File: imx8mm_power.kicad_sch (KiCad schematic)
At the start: 4 parts, among them U3 MT40A1G16KD-062E

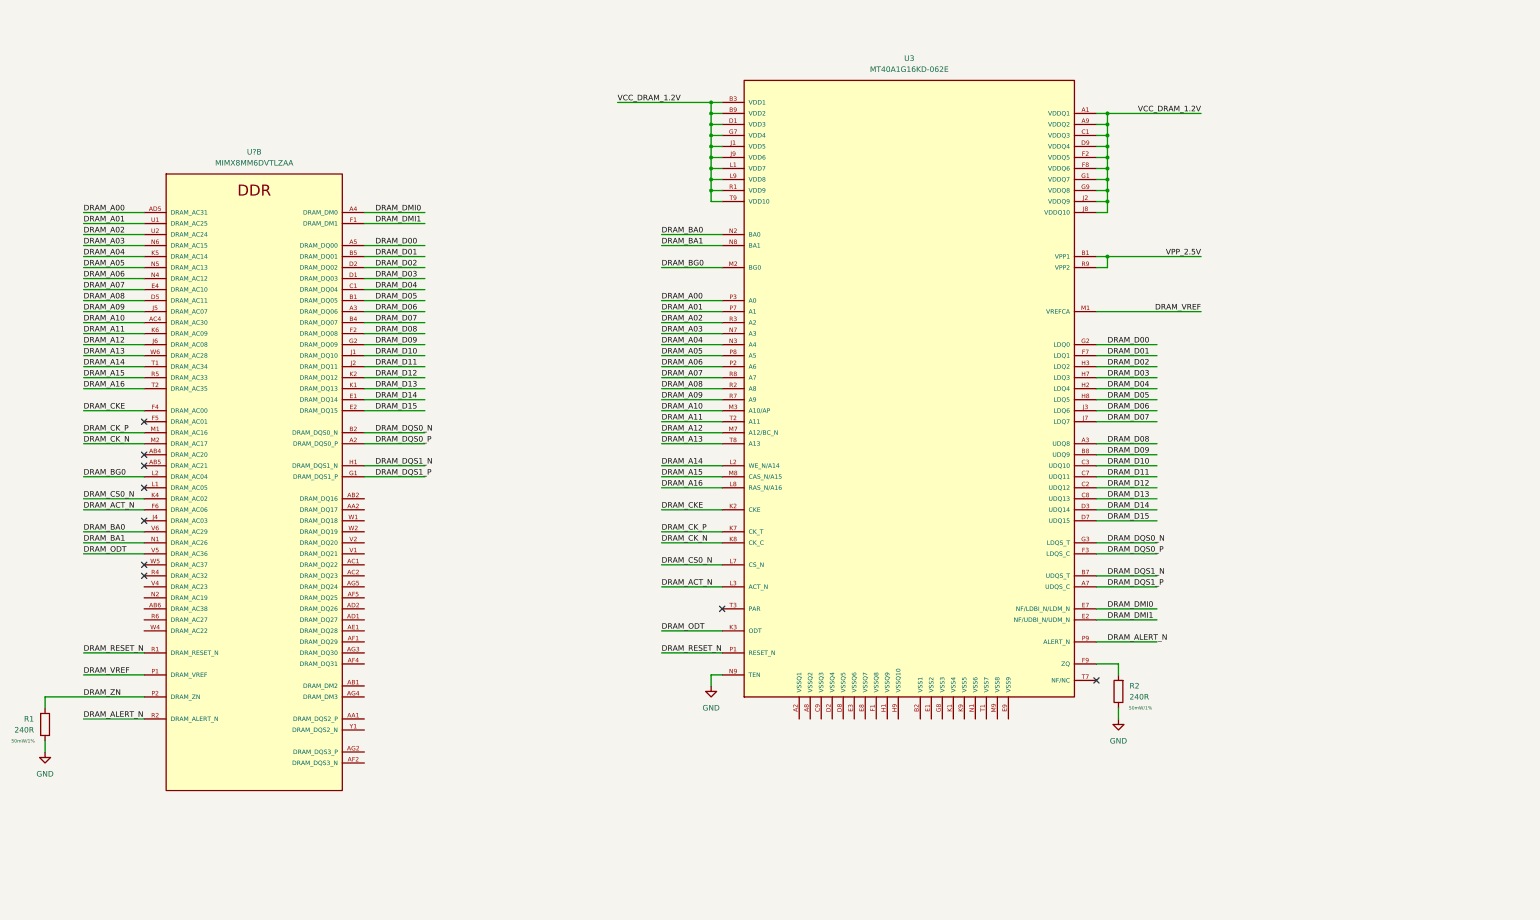
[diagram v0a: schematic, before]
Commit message: move to i.MX8M Mini
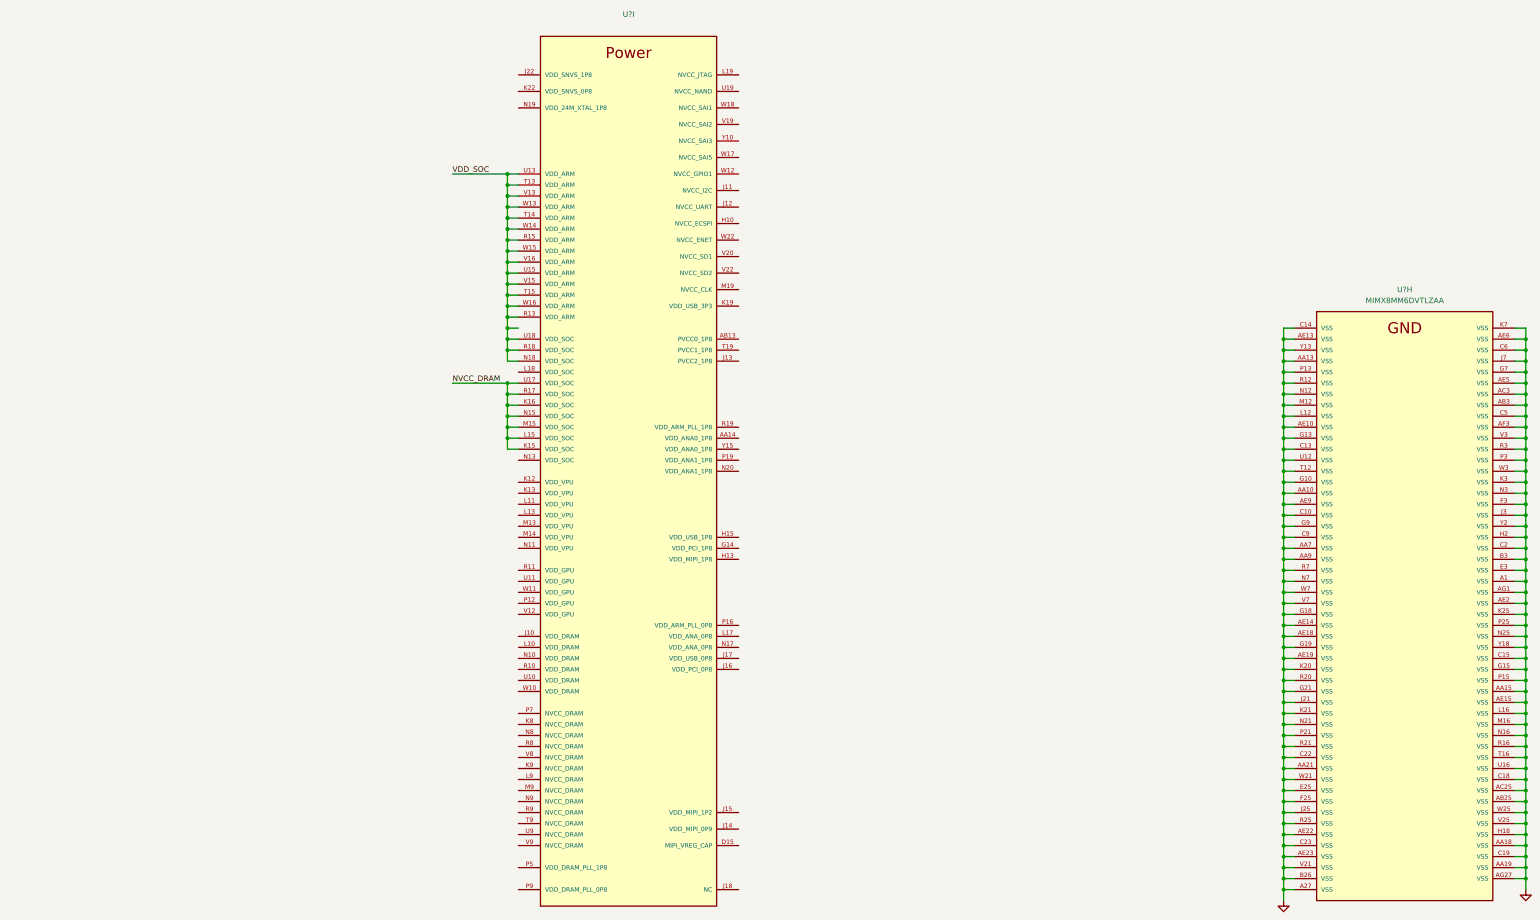
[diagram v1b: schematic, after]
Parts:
- removed R1, R2: 240R, symbol Device:R
- removed U3: MT40A1G16KD-062E, qsbc:MICRON-FBGA-96, symbol qsbc:MT40A1G16KD-062E
- removed U?: MIMX8MM6DVTLZAA, qsbc:SOT1967-1, symbol qsbc:MIMX8MM6DVTLZAA
- added U?: MIMX8MM6DVTLZAA, qsbc:SOT1967-1, symbol qsbc:MIMX8MM6DVTLZAA
- added U?: (no value), symbol qsbc:MIMX8MM6DVTLZAA
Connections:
- net GND: now also U?.A1 (VSS), U?.A27 (VSS), U?.AA10 (VSS), U?.AA13 (VSS), U?.AA15 (VSS), U?.AA18 (VSS), U?.AA19 (VSS), U?.AA21 (VSS), U?.AA7 (VSS), U?.AA9 (VSS), U?.AB25 (VSS), U?.AB3 (VSS), U?.AC25 (VSS), U?.AC3 (VSS), U?.AE10 (VSS), U?.AE13 (VSS), U?.AE14 (VSS), U?.AE15 (VSS), U?.AE18 (VSS), U?.AE19 (VSS), U?.AE2 (VSS), U?.AE22 (VSS), U?.AE23 (VSS), U?.AE5 (VSS), U?.AE6 (VSS), U?.AE9 (VSS), U?.AF3 (VSS), U?.AG1 (VSS), U?.AG27 (VSS), U?.B26 (VSS), U?.B3 (VSS), U?.C10 (VSS), U?.C13 (VSS), U?.C14 (VSS), U?.C15 (VSS), U?.C18 (VSS), U?.C19 (VSS), U?.C2 (VSS), U?.C22 (VSS), U?.C23 (VSS), U?.C5 (VSS), U?.C6 (VSS), U?.C9 (VSS), U?.E25 (VSS), U?.E3 (VSS), U?.F25 (VSS), U?.F3 (VSS), U?.G10 (VSS), U?.G13 (VSS), U?.G15 (VSS), U?.G18 (VSS), U?.G19 (VSS), U?.G21 (VSS), U?.G7 (VSS), U?.G9 (VSS), U?.H18 (VSS), U?.H2 (VSS), U?.J21 (VSS), U?.J25 (VSS), U?.J3 (VSS), U?.J7 (VSS), U?.K20 (VSS), U?.K21 (VSS), U?.K25 (VSS), U?.K3 (VSS), U?.K7 (VSS), U?.L12 (VSS), U?.L16 (VSS), U?.M12 (VSS), U?.M16 (VSS), U?.N12 (VSS), U?.N16 (VSS), U?.N21 (VSS), U?.N25 (VSS), U?.N3 (VSS), U?.N7 (VSS), U?.P13 (VSS), U?.P15 (VSS), U?.P21 (VSS), U?.P25 (VSS), U?.P3 (VSS), U?.R12 (VSS), U?.R16 (VSS), U?.R20 (VSS), U?.R21 (VSS), U?.R25 (VSS), U?.R3 (VSS), U?.R7 (VSS), U?.T12 (VSS), U?.T16 (VSS), U?.U12 (VSS), U?.U16 (VSS), U?.V21 (VSS), U?.V25 (VSS), U?.V3 (VSS), U?.V7 (VSS), U?.W21 (VSS), U?.W25 (VSS), U?.W3 (VSS), U?.W7 (VSS), U?.Y13 (VSS), U?.Y18 (VSS), U?.Y2 (VSS)
- new net NVCC_DRAM: U?.K15 (VDD_SOC), U?.K16 (VDD_SOC), U?.L15 (VDD_SOC), U?.M15 (VDD_SOC), U?.N15 (VDD_SOC), U?.R17 (VDD_SOC), U?.U17 (VDD_SOC)
- new net VDD_SOC: U?.N18 (VDD_SOC), U?.R13 (VDD_ARM), U?.R15 (VDD_ARM), U?.R18 (VDD_SOC), U?.T13 (VDD_ARM), U?.T14 (VDD_ARM), U?.T15 (VDD_ARM), U?.U13 (VDD_ARM), U?.U15 (VDD_ARM), U?.U18 (VDD_SOC), U?.V13 (VDD_ARM), U?.V15 (VDD_ARM), U?.V16 (VDD_ARM), U?.W13 (VDD_ARM), U?.W14 (VDD_ARM), U?.W15 (VDD_ARM), U?.W16 (VDD_ARM)
- no-connect marks 9 -> 0

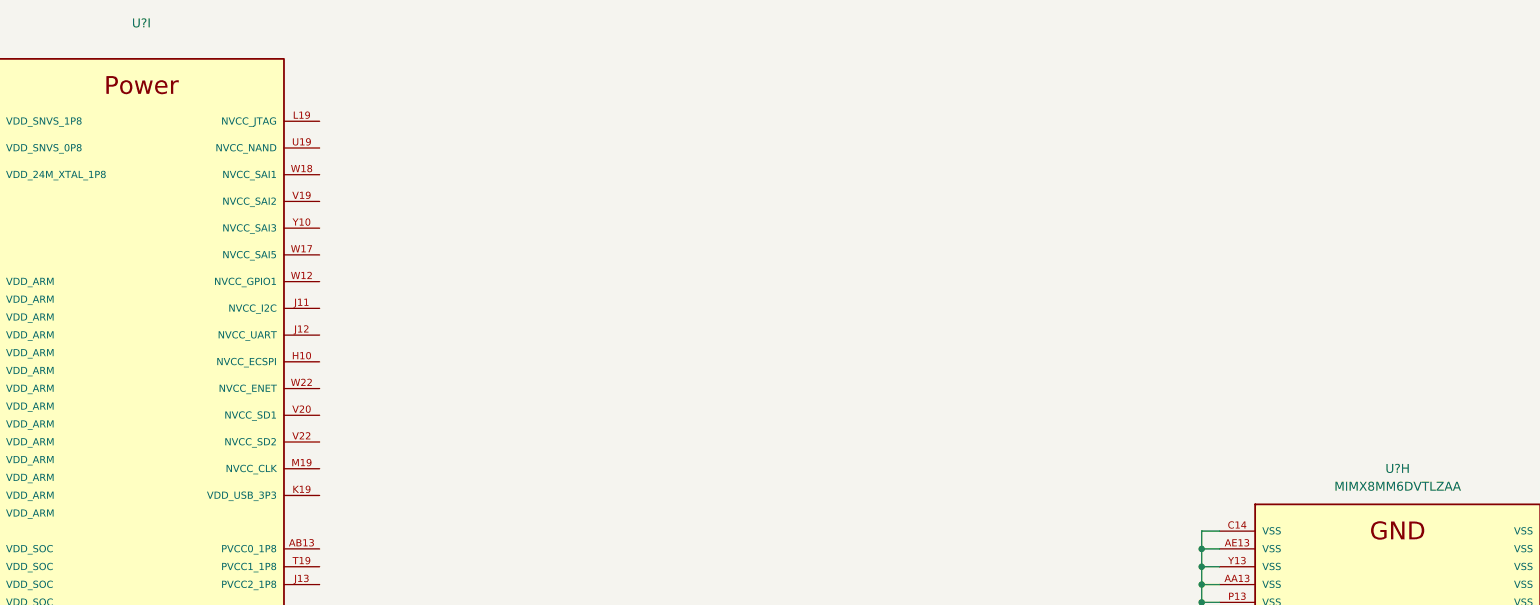
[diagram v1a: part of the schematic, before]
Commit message: ddr sch done
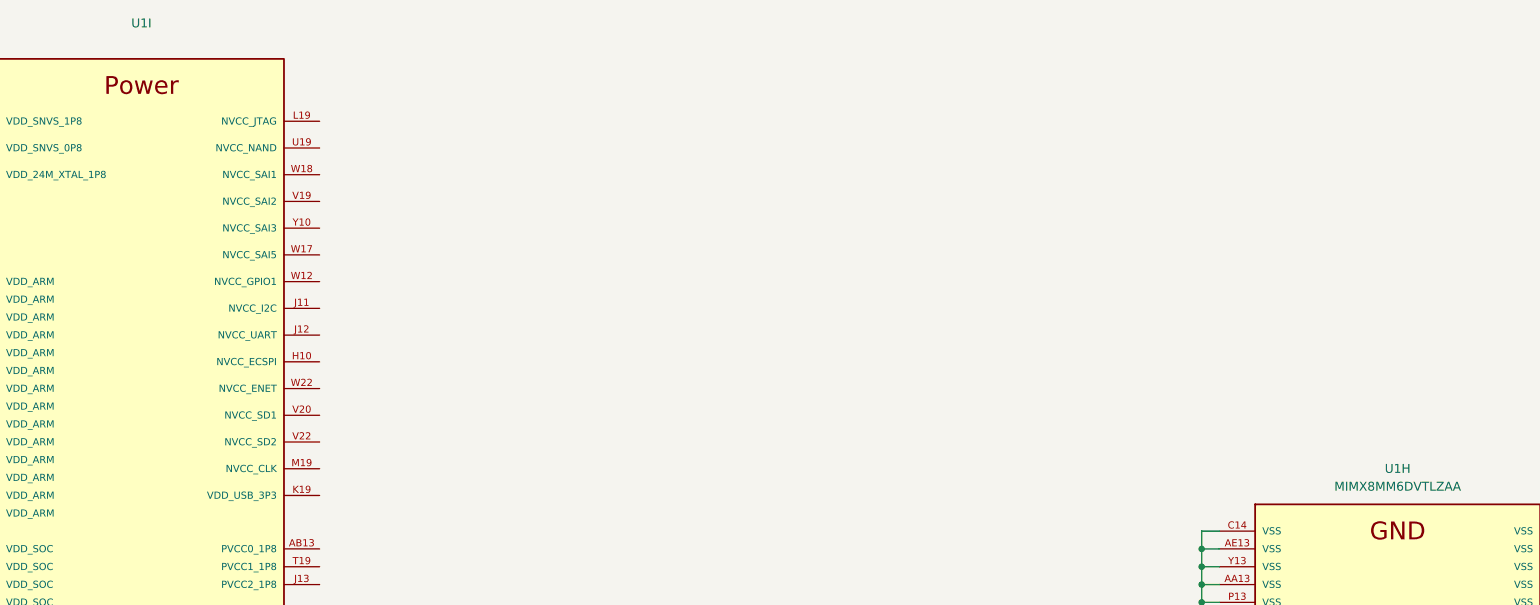
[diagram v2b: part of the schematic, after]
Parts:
- gave numbers to parts that had none: 1
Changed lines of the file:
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@@
   (symbol (lib_id "qsbc:MIMX8MM6DVTLZAA") (at 365.76 115.57 0) (unit 8)
     (in_bom yes) (on_board yes) (fields_autoplaced)
-    (property "Reference" "U?" (id 0) (at 365.76 96.52 0))
+    (property "Reference" "U1" (id 0) (at 365.76 96.52 0))
     (property "Value" "MIMX8MM6DVTLZAA" (id 1) (at 365.76 99.06 0))
     (property "Footprint" "qsbc:SOT1967-1" (id 2) (at 369.57 306.07 0)
@@
   (symbol (lib_id "qsbc:MIMX8MM6DVTLZAA") (at 186.69 52.07 0) (unit 9)
     (in_bom yes) (on_board yes) (fields_autoplaced)
-    (property "Reference" "U?" (id 0) (at 186.69 33.02 0))
+    (property "Reference" "U1" (id 0) (at 186.69 33.02 0))
     (property "Value" "" (id 1) (at 186.69 35.56 0))
     (property "Footprint" "" (id 2) (at 190.5 242.57 0)

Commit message: misc work, usb sch done
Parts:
- U1: value (none) -> MIMX8MM6DVTLZAA; footprint (none) -> qsbc:SOT1967-1
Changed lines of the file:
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@@
       (effects (font (size 1.27 1.27)) hide)
     )
-    (property "Value" "" (id 1) (at 337.82 242.57 0))
+    (property "Value" "GND" (id 1) (at 337.82 242.57 0))
     (property "Footprint" "" (id 2) (at 337.82 237.49 0)
       (effects (font (size 1.27 1.27)) hide)
@@
       (effects (font (size 1.27 1.27)) hide)
     )
-    (property "Value" "" (id 1) (at 393.7 240.03 0))
+    (property "Value" "GND" (id 1) (at 393.7 240.03 0))
     (property "Footprint" "" (id 2) (at 393.7 234.95 0)
       (effects (font (size 1.27 1.27)) hide)
@@
     (in_bom yes) (on_board yes) (fields_autoplaced)
     (property "Reference" "U1" (id 0) (at 186.69 33.02 0))
-    (property "Value" "" (id 1) (at 186.69 35.56 0))
-    (property "Footprint" "" (id 2) (at 190.5 242.57 0)
+    (property "Value" "MIMX8MM6DVTLZAA" (id 1) (at 186.69 35.56 0))
+    (property "Footprint" "qsbc:SOT1967-1" (id 2) (at 190.5 242.57 0)
       (effects (font (size 1.27 1.27)) (justify left bottom) hide)
     )

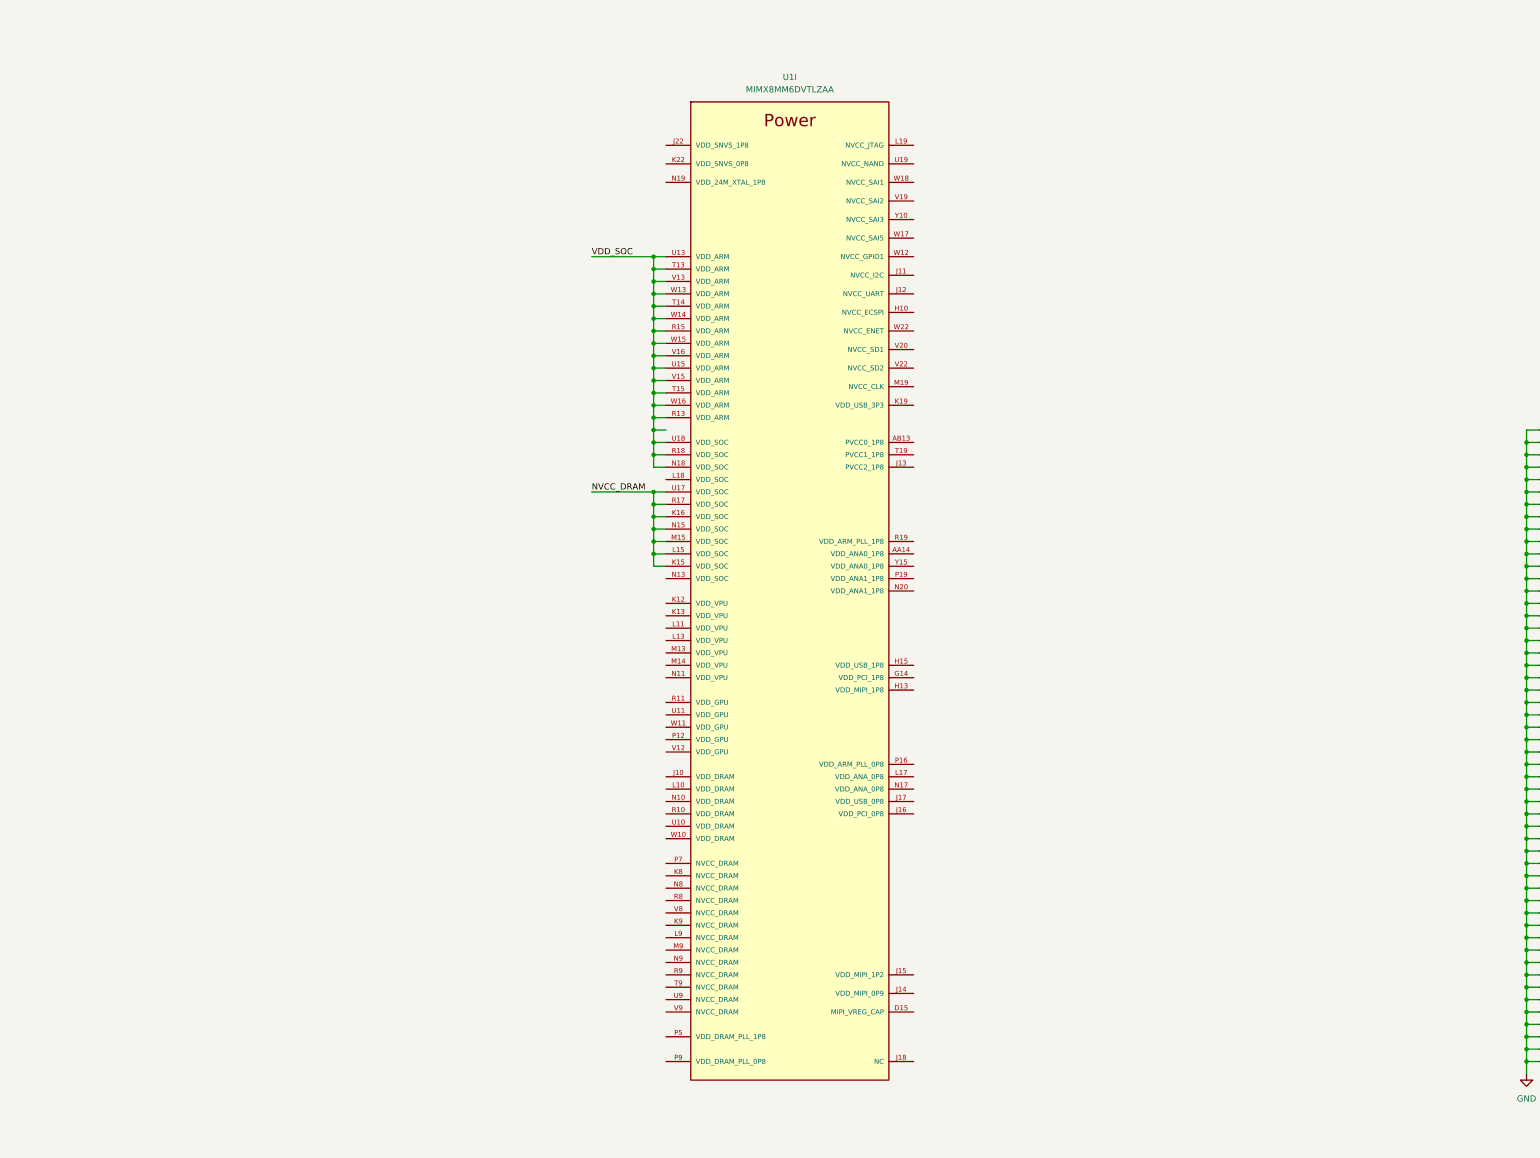
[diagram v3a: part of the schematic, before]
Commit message: enet sch done, other misc sch work
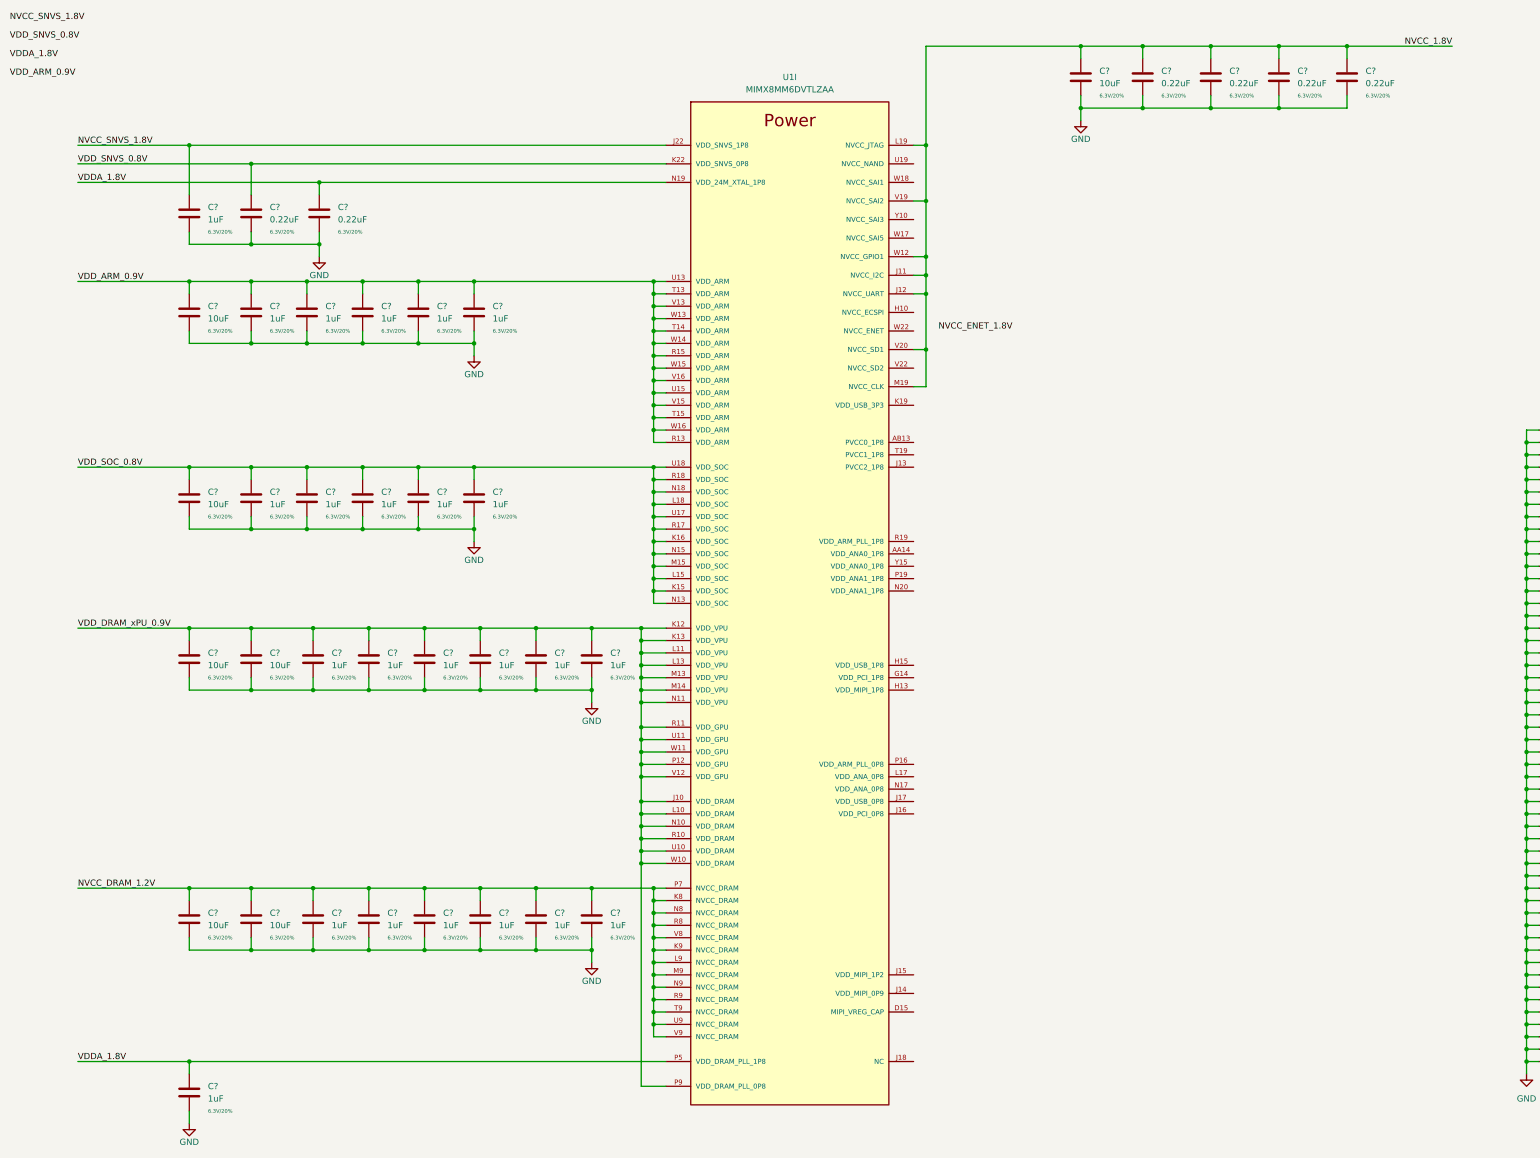
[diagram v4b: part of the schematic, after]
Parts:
- added C? (x24): 1uF, Capacitor_SMD:C_0201_0603Metric, symbol Device:C
- added C? (x7): 10uF, Capacitor_SMD:C_0402_1005Metric, symbol Device:C
- added C? (x6): 0.22uF, Capacitor_SMD:C_0201_0603Metric, symbol Device:C
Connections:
- net NVCC_DRAM is gone; now on net VDD_SOC_0.8V: U1.K15 (VDD_SOC), U1.K16 (VDD_SOC), U1.L15 (VDD_SOC), U1.M15 (VDD_SOC), U1.N15 (VDD_SOC), U1.R17 (VDD_SOC), U1.U17 (VDD_SOC)
- net GND: now also C?.2, C?.2, C?.2, C?.2, C?.2, C?.2, C?.2, C?.2, C?.2, C?.2, C?.2, C?.2, C?.2, C?.2, C?.2, C?.2, C?.2, C?.2, C?.2, C?.2, C?.2, C?.2, C?.2, C?.2, C?.2, C?.2, C?.2, C?.2, C?.2, C?.2, C?.2, C?.2, C?.2, C?.2, C?.2, C?.2, C?.2
- net VDD_DRAM_xPU_0.9V: now reaches U1.J10 (VDD_DRAM)
- net VDD_DRAM_xPU_0.9V: now also U1.K12 (VDD_VPU), U1.K13 (VDD_VPU), U1.L10 (VDD_DRAM), U1.L11 (VDD_VPU), U1.L13 (VDD_VPU), U1.M13 (VDD_VPU), U1.M14 (VDD_VPU), U1.N10 (VDD_DRAM), U1.N11 (VDD_VPU), U1.P12 (VDD_GPU), U1.P9 (VDD_DRAM_PLL_0P8), U1.R10 (VDD_DRAM), U1.R11 (VDD_GPU), U1.U10 (VDD_DRAM), U1.U11 (VDD_GPU), U1.V12 (VDD_GPU), U1.W10 (VDD_DRAM), U1.W11 (VDD_GPU), C?.1, C?.1, C?.1, C?.1, C?.1, C?.1, C?.1, C?.1
- net NVCC_1.8V: now reaches U1.J11 (NVCC_I2C)
- net NVCC_1.8V: now also U1.J12 (NVCC_UART), U1.L19 (NVCC_JTAG), U1.M19 (NVCC_CLK), U1.V19 (NVCC_SAI2), U1.V20 (NVCC_SD1), U1.W12 (NVCC_GPIO1), C?.1, C?.1, C?.1, C?.1, C?.1
- net NVCC_SNVS_1.8V: now reaches U1.J22 (VDD_SNVS_1P8)
- net NVCC_SNVS_1.8V: now also C?.1
- net VDD_SNVS_0.8V: now reaches U1.K22 (VDD_SNVS_0P8)
- net VDD_SNVS_0.8V: now also C?.1
- net NVCC_DRAM_1.2V: now reaches U1.K8 (NVCC_DRAM)
- net NVCC_DRAM_1.2V: now also U1.K9 (NVCC_DRAM), U1.L9 (NVCC_DRAM), U1.M9 (NVCC_DRAM), U1.N8 (NVCC_DRAM), U1.N9 (NVCC_DRAM), U1.P7 (NVCC_DRAM), U1.R8 (NVCC_DRAM), U1.R9 (NVCC_DRAM), U1.T9 (NVCC_DRAM), U1.U9 (NVCC_DRAM), U1.V8 (NVCC_DRAM), U1.V9 (NVCC_DRAM), C?.1, C?.1, C?.1, C?.1, C?.1, C?.1, C?.1, C?.1
- net VDD_SOC_0.8V: now reaches U1.L18 (VDD_SOC)
- net VDD_SOC_0.8V: now also U1.N13 (VDD_SOC), U1.N18 (VDD_SOC), U1.R18 (VDD_SOC), U1.U18 (VDD_SOC), C?.1, C?.1, C?.1, C?.1, C?.1, C?.1
- net VDDA_1.8V: now reaches U1.N19 (VDD_24M_XTAL_1P8)
- net VDDA_1.8V: now also U1.P5 (VDD_DRAM_PLL_1P8), C?.1, C?.1
- net VDD_SOC renamed VDD_ARM_0.9V
- net VDD_ARM_0.9V: now also C?.1, C?.1, C?.1, C?.1, C?.1, C?.1; no longer U1.N18 (VDD_SOC), U1.R18 (VDD_SOC), U1.U18 (VDD_SOC)
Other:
- moved on the sheet: U1I
